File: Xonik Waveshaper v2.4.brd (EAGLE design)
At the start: 55.9 x 21 mm, 78 parts, among them IC1 TL074JT, IC2 TL074JT, IC3 TL074JT, IC5 4013T, IC7 78L05F, IC8 TL074JT, T1 2n3904

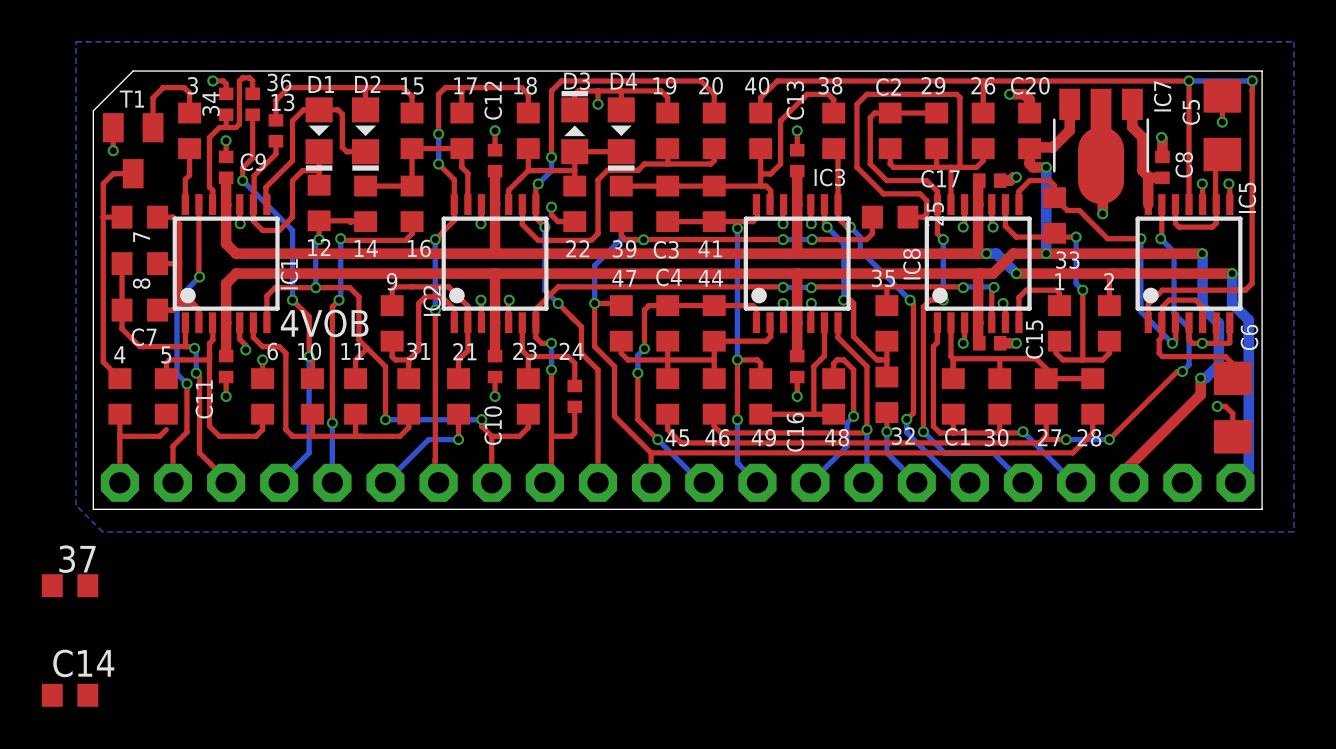
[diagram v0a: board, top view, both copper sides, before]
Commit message: Preparing for doing 4 layer board
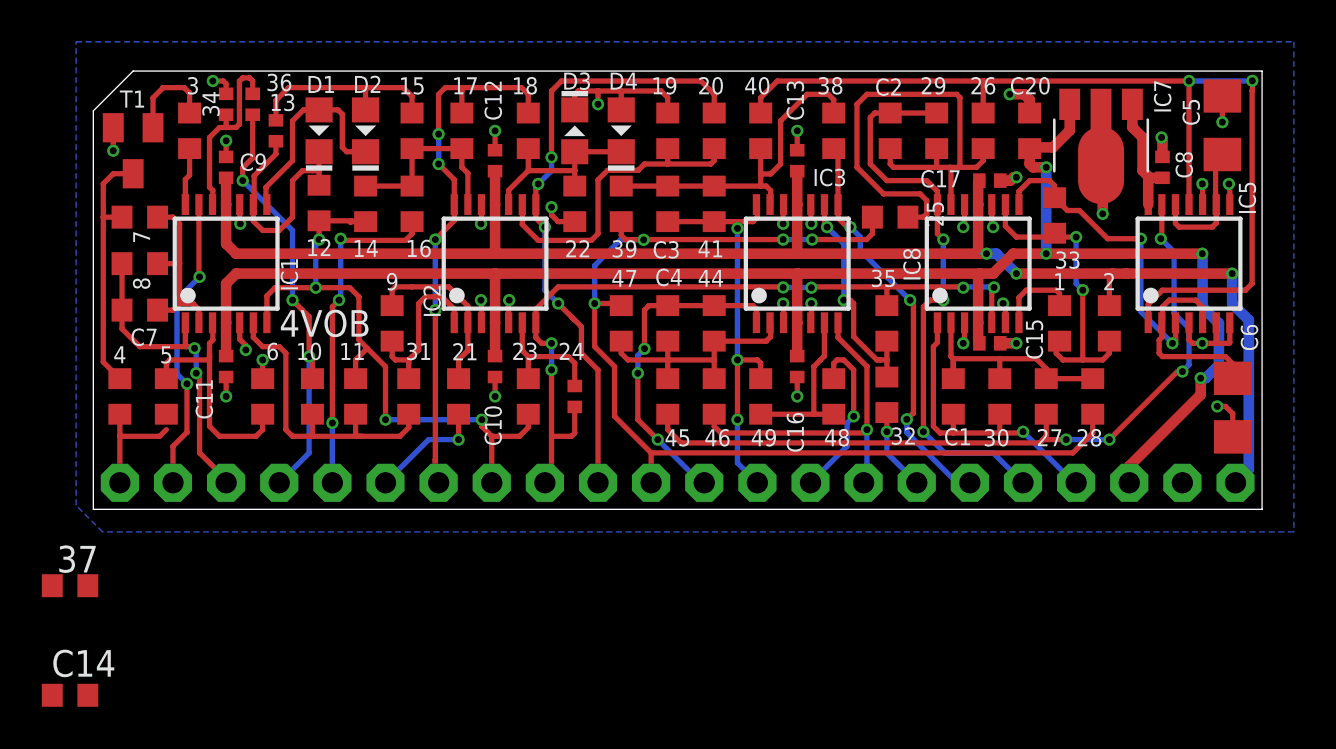
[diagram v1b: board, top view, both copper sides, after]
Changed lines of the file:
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@@
 <layers>
 <layer number="1" name="Top" color="4" fill="1" visible="no" active="yes"/>
-<layer number="2" name="Route2" color="1" fill="3" visible="no" active="no"/>
+<layer number="2" name="Route2" color="1" fill="3" visible="no" active="yes"/>
 <layer number="3" name="Route3" color="4" fill="3" visible="no" active="no"/>
 <layer number="14" name="Route14" color="1" fill="6" visible="no" active="no"/>
-<layer number="15" name="Route15" color="4" fill="6" visible="no" active="no"/>
+<layer number="15" name="Route15" color="4" fill="6" visible="no" active="yes"/>
 <layer number="16" name="Bottom" color="1" fill="1" visible="yes" active="yes"/>
 <layer number="17" name="Pads" color="2" fill="1" visible="yes" active="yes"/>
@@
 <layer number="20" name="Dimension" color="15" fill="1" visible="yes" active="yes"/>
 <layer number="21" name="tPlace" color="7" fill="1" visible="no" active="yes"/>
-<layer number="22" name="bPlace" color="7" fill="1" visible="yes" active="yes"/>
+<layer number="22" name="bPlace" color="7" fill="1" visible="no" active="yes"/>
 <layer number="23" name="tOrigins" color="15" fill="1" visible="no" active="yes"/>
 <layer number="24" name="bOrigins" color="15" fill="1" visible="yes" active="yes"/>
@@
 <layer number="38" name="bTest" color="7" fill="1" visible="no" active="yes"/>
 <layer number="39" name="tKeepout" color="4" fill="11" visible="no" active="yes"/>
-<layer number="40" name="bKeepout" color="1" fill="11" visible="yes" active="yes"/>
+<layer number="40" name="bKeepout" color="1" fill="11" visible="no" active="yes"/>
 <layer number="41" name="tRestrict" color="4" fill="10" visible="no" active="yes"/>
-<layer number="42" name="bRestrict" color="1" fill="10" visible="yes" active="yes"/>
+<layer number="42" name="bRestrict" color="1" fill="10" visible="no" active="yes"/>
 <layer number="43" name="vRestrict" color="2" fill="10" visible="no" active="yes"/>
 <layer number="44" name="Drills" color="7" fill="1" visible="no" active="yes"/>
@@
 <layer number="50" name="dxf" color="7" fill="1" visible="no" active="no"/>
 <layer number="51" name="tDocu" color="7" fill="1" visible="no" active="yes"/>
-<layer number="52" name="bDocu" color="7" fill="1" visible="yes" active="yes"/>
+<layer number="52" name="bDocu" color="7" fill="1" visible="no" active="yes"/>
 <layer number="53" name="tGND_GNDA" color="7" fill="9" visible="no" active="no"/>
 <layer number="54" name="bGND_GNDA" color="1" fill="9" visible="no" active="no"/>
@@
 </class>
 </classes>
-<designrules name="jlcpcb-2layers *">
-<description language="en">&lt;b&gt;JLCPCB design rules (2 layers)&lt;/b&gt;
+<designrules name="jlcpcb-4layers">
+<description language="en">&lt;b&gt;JLCPCB design rules (4 layers)&lt;/b&gt;
 &lt;ul&gt;
 &lt;li&gt;Board thickness: 1.6mm&lt;/li&gt;
-&lt;li&gt;Copper weight: 1oz (35um)&lt;/li&gt;
+&lt;li&gt;Copper weight: outer layers: 1oz (35um), inner layers: 0.5oz (16.5um)&lt;/li&gt;
 &lt;li&gt;Note: annular ring aren't minimal&lt;/li&gt;
 &lt;/ul&gt;</description>
-<param name="layerSetup" value="(1*16)"/>
-<param name="mtCopper" value="0.035mm 0.035mm 0.035mm 0.035mm 0.035mm 0.035mm 0.035mm 0.035mm 0.035mm 0.035mm 0.035mm 0.035mm 0.035mm 0.035mm 0.035mm 0.035mm"/>
-<param name="mtIsolate" value="1.6mm 0.15mm 0.2mm 0.15mm 0.2mm 0.15mm 0.2mm 0.15mm 0.2mm 0.15mm 0.2mm 0.15mm 0.2mm 0.15mm 0.2mm"/>
-<param name="mdWireWire" value="5mil"/>
+<param name="layerSetup" value="(1+2*15+16)"/>
+<param name="mtCopper" value="0.035mm 0.0175mm 0.035mm 0.035mm 0.035mm 0.035mm 0.035mm 0.035mm 0.035mm 0.035mm 0.035mm 0.035mm 0.035mm 0.035mm 0.0175mm 0.035mm"/>
+<param name="mtIsolate" value="0.2mm 1.065mm 0.2mm 0.15mm 0.2mm 0.15mm 0.2mm 0.15mm 0.2mm 0.15mm 0.2mm 0.15mm 0.2mm 0.15mm 0.2mm"/>
+<param name="mdWireWire" value="3.5mil"/>
 <param name="mdWirePad" value="5mil"/>
-<param name="mdWireVia" value="5mil"/>
+<param name="mdWireVia" value="0.2mm"/>
 <param name="mdPadPad" value="5mil"/>
 <param name="mdPadVia" value="5mil"/>
@@
 <param name="mdDrill" value="6mil"/>
 <param name="mdSmdStop" value="0mil"/>
-<param name="msWidth" value="5mil"/>
-<param name="msDrill" value="0.3mm"/>
-<param name="msMicroVia" value="0.3mm"/>
+<param name="msWidth" value="3.5mil"/>
+<param name="msDrill" value="0.2mm"/>
+<param name="msMicroVia" value="0.2mm"/>
 <param name="msBlindViaRatio" value="0.5"/>
 <param name="rvPadTop" value="0.4"/>
@@
 <param name="rlMinPadBottom" value="10mil"/>
 <param name="rlMaxPadBottom" value="80mil"/>
-<param name="rlMinViaOuter" value="4mil"/>
+<param name="rlMinViaOuter" value="0.13mm"/>
 <param name="rlMaxViaOuter" value="20mil"/>
 <param name="rlMinViaInner" value="8mil"/>
@@
 <param name="mvStopFrame" value="1"/>
 <param name="mvCreamFrame" value="0"/>
-<param name="mlMinStopFrame" value="4mil"/>
-<param name="mlMaxStopFrame" value="4mil"/>
+<param name="mlMinStopFrame" value="0.05mm"/>
+<param name="mlMaxStopFrame" value="0.05mm"/>
 <param name="mlMinCreamFrame" value="0mil"/>
 <param name="mlMaxCreamFrame" value="0mil"/>
-<param name="mlViaStopLimit" value="0mil"/>
+<param name="mlViaStopLimit" value="16mil"/>
 <param name="srRoundness" value="0"/>
 <param name="srMinRoundness" value="0mil"/>
@@
 <wire x1="48.26" y1="19.03075" x2="48.26" y2="16.36375" width="0.508" layer="1"/>
 <contactref element="C14" pad="1"/>
-<wire x1="54.2925" y1="15.5575" x2="53.98135" y2="18.51025" width="0" layer="19" extent="1-1"/>
-<wire x1="53.0225" y1="15.5575" x2="54.2925" y2="15.5575" width="0" layer="19" extent="1-1"/>
-<wire x1="51.1175" y1="16.85125" x2="53.0225" y2="15.5575" width="0" layer="19" extent="1-1"/>
-<wire x1="48.180625" y1="16.443125" x2="51.1175" y2="16.85125" width="0" layer="19" extent="1-1"/>
-<wire x1="44.7675" y1="18.9475" x2="48.180625" y2="19.110125" width="0" layer="19" extent="1-1"/>
-<wire x1="44.1325" y1="15.875" x2="44.7675" y2="18.9475" width="0" layer="19" extent="1-1"/>
-<wire x1="42.956875" y1="14.5725" x2="43.3625" y2="15.71625" width="0" layer="19" extent="1-1"/>
-<wire x1="41.656875" y1="14.5725" x2="42.956875" y2="14.5725" width="0" layer="19" extent="1-1"/>
-<wire x1="43.4975" y1="9.8425" x2="43.02125" y2="13.49375" width="0" layer="19" extent="1-1"/>
-<wire x1="43.3625" y1="7.9375" x2="43.606875" y2="8.9225" width="0" layer="19" extent="1-1"/>
-<wire x1="41.5925" y1="7.9375" x2="43.3625" y2="7.9375" width="0" layer="19" extent="1-1"/>
-<wire x1="54.3375" y1="8.9225" x2="54.3375" y2="14.5725" width="0" layer="19" extent="1-1"/>
-<wire x1="53.736875" y1="4.92125" x2="53.0225" y2="7.9375" width="0" layer="19" extent="1-1"/>
-<wire x1="52.07" y1="1.27" x2="54.47665" y2="3.4641" width="0" layer="19" extent="1-1"/>
-<wire x1="34.3296875" y1="13.6525" x2="41.5925" y2="13.49375" width="0" layer="19" extent="1-1"/>
-<wire x1="33.005" y1="14.5725" x2="34.305" y2="14.5725" width="0" layer="19" extent="1-1"/>
-<wire x1="33.655" y1="17.16875" x2="34.305" y2="14.5725" width="0" layer="19" extent="1-1"/>
-<wire x1="34.3296875" y1="9.8425" x2="34.3296875" y2="13.6525" width="0" layer="19" extent="1-1"/>
-<wire x1="33.005" y1="8.9225" x2="34.305" y2="8.9225" width="0" layer="19" extent="1-1"/>
-<wire x1="33.655" y1="6.32625" x2="34.305" y2="8.9225" width="0" layer="19" extent="1-1"/>
-<wire x1="27.46375" y1="18.9475" x2="33.655" y2="18.0975" width="0" layer="19" extent="1-1"/>
-<wire x1="19.20875" y1="18.0975" x2="23.01875" y2="19.0975" width="0" layer="19" extent="1-1"/>
-<wire x1="18.55875" y1="14.5725" x2="19.20875" y2="17.16875" width="0" layer="19" extent="1-1"/>
-<wire x1="21.9075" y1="14.44625" x2="18.55875" y2="14.5725" width="0" layer="19" extent="1-1"/>
-<wire x1="18.5340625" y1="10.00125" x2="18.5340625" y2="13.6525" width="0" layer="19" extent="1-1"/>
-<wire x1="19.85875" y1="8.9225" x2="18.55875" y2="8.9225" width="0" layer="19" extent="1-1"/>
-<wire x1="19.20875" y1="6.32625" x2="18.55875" y2="8.9225" width="0" layer="19" extent="1-1"/>
-<wire x1="8.09625" y1="7.14375" x2="18.55875" y2="8.9225" width="0" layer="19" extent="1-1"/>
-<wire x1="7.2898" y1="7.62" x2="8.09625" y2="7.14375" width="0" layer="19" extent="1-1"/>
-<wire x1="6.35" y1="6.32625" x2="7.2898" y2="7.62" width="0" layer="19" extent="1-1"/>
-<wire x1="7.0246875" y1="13.6525" x2="7" y2="8.9225" width="0" layer="19" extent="1-1"/>
-<wire x1="6.35" y1="16.85125" x2="7" y2="14.5725" width="0" layer="19" extent="1-1"/>
-<wire x1="6.35" y1="19.8675" x2="6.35" y2="17.62125" width="0" layer="19" extent="1-1"/>
-<wire x1="0.955" y1="18.245" x2="5.715" y2="20.47875" width="0" layer="19" extent="1-1"/>
-<wire x1="-1.96125" y1="-8.89" x2="6.35" y2="5.3975" width="0" layer="19" extent="1-1"/>
+<wire x1="6.35" y1="5.3975" x2="-1.96125" y2="-8.89" width="0" layer="19" extent="1-1"/>
 </signal>
 <signal name="N$2">

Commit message: Converted to 4 layer and fixed all issues
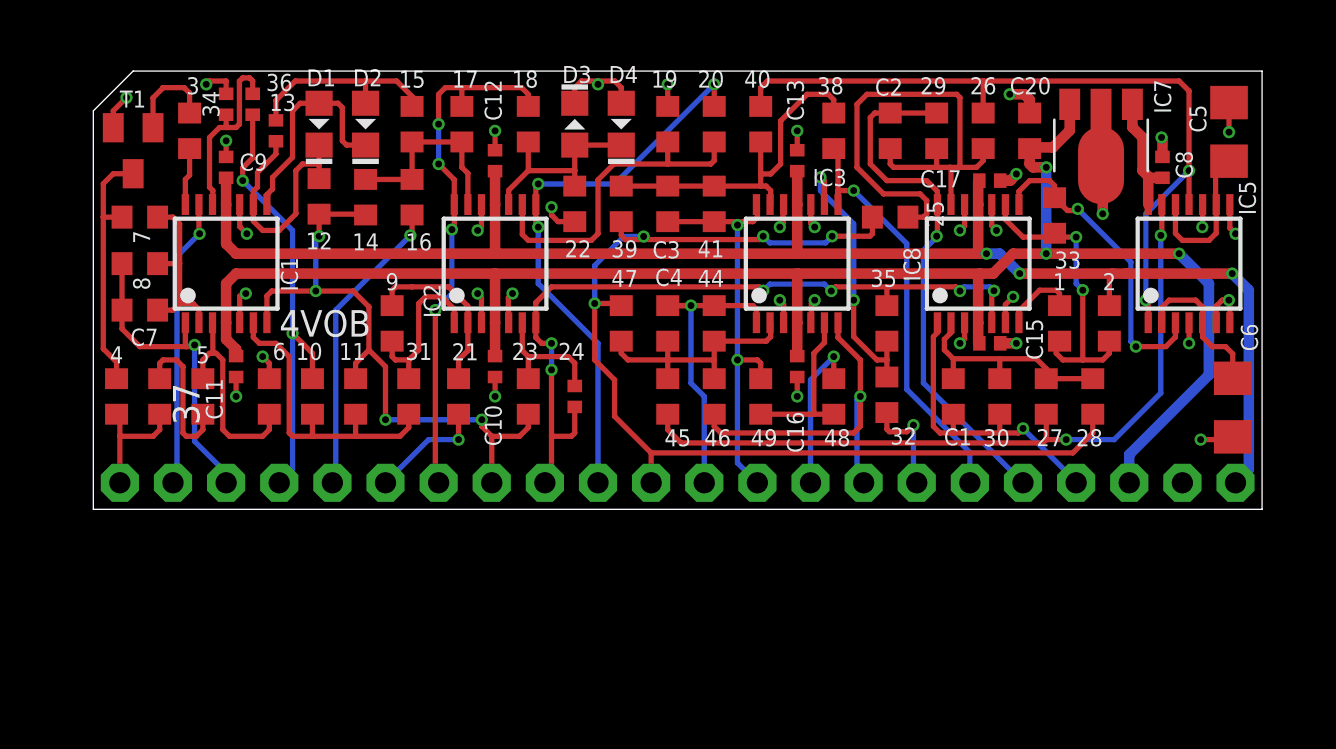
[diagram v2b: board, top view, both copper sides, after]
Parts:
- removed C14: 100pF-DNM, joakim:C0603-J
- moved 37 10.0 mm to (3.17, 5.40), turned to 270 degrees
- moved 5 1.75 mm to (5.24, 5.40)
- moved C11 0.48 mm to (6.83, 6.83)
- moved C5 0.45 mm to (54.3, 18.0)
- moved 12 0.32 mm to (10.8, 15.0)
- moved 6 0.32 mm to (8.41, 5.40)
- moved 14 0.32 mm to (13.0, 14.9)
- moved 15 0.32 mm to (15.2, 18.4)
- moved 16 0.32 mm to (15.2, 14.9)
- moved 17 0.32 mm to (17.6, 18.4)
- moved 18 0.32 mm to (20.8, 18.4)
- moved 19 0.32 mm to (27.5, 18.4)
- moved 20 0.32 mm to (29.7, 18.4)
- moved 40 0.32 mm to (31.9, 18.4)
- moved D1 0.32 mm to (10.8, 18.4)
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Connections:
- net GND: no longer C14.1
- net N$3: no longer C14.2
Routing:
- net N$32: track 48.0 -> 36.8 mm
- net N$16: track 0.00 -> 7.11 mm
- net SINE: track 29.6 -> 27.0 mm, vias 4 -> 3
- net N$31: track 9.64 -> 7.34 mm
- net N$24: track 11.3 -> 13.6 mm
- net SUB_SQR_1: track 27.4 -> 25.5 mm, vias 3 -> 1
- net GND: track 50.6 -> 52.6 mm, vias 34 -> 36
- net N$5: track 11.8 -> 10.1 mm
- net SYMMETRY: track 16.0 -> 14.4 mm, vias 3 -> 1
- net SUB_SAW_2: track 16.1 -> 14.8 mm, vias 3 -> 1
- net N$35: track 37.0 -> 35.8 mm, vias 4 -> 2
- net SS1_TRIM_L: track 3.99 -> 5.09 mm
- net SS2_TRIM_R: track 16.5 -> 17.5 mm
- net SS1_TRIM_R: track 19.4 -> 20.4 mm, vias 3 -> 1
- net N$34: track 6.54 -> 7.54 mm
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- added copper zone on layer 15, net GND
- added copper zone on layer 2, net GND
- removed copper zone on layer 16, net GND
